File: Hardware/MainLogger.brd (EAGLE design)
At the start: 98.9 x 72.1 mm, 258 parts, among them J3 GEMS_POWER_PLUGINPUT_RT, J4 U.FL, J5 SIM_CDNANO_SF72, P1:C1 0.1uF, P1:C2 2.2uF, P1:C3 1uF, P1:C4 100uF, P1:C5 0.1uF, P1:J1 CONN_TALON_LOGGER, P1:R2 1k, P1:R3 1k, P1:U1 SN74AUP1G08DCK, P1:U2 FXMAR2102UMLP, P1:U3 FSA2258, P1:U4 AP2411, P2:C1 0.1uF, P2:C2 2.2uF, P2:C3 1uF, P2:C4 100uF, P2:C5 0.1uF, P2:J1 CONN_TALON_LOGGER, P2:R2 1k, P2:R3 1k, P2:U1 SN74AUP1G08DCK, P2:U2 FXMAR2102UMLP, P2:U3 FSA2258, P2:U4 AP2411, P3:C1 0.1uF, P3:C2 2.2uF, P3:C3 1uF, P3:C4 100uF, P3:C5 0.1uF, P3:J1 CONN_TALON_LOGGER, P3:R2 1k, P3:R3 1k, P3:U1 SN74AUP1G08DCK, P3:U2 FXMAR2102UMLP, P3:U3 FSA2258, P3:U4 AP2411, P4:C1 0.1uF, P4:C2 2.2uF, P4:C3 1uF, P4:C4 100uF, P4:C5 0.1uF, P4:J1 CONN_TALON_LOGGER, P4:R2 1k, P4:R3 1k, P4:U1 SN74AUP1G08DCK, P4:U2 FXMAR2102UMLP, P4:U3 FSA2258, P4:U4 AP2411, Q1 DMG3404, Q2 MOSFET_PCH-DMP3036SFG, Q3 MOSFET_PCH-DMP3036SFG, Q4 DMG3404, Q5 NX2301P, Q6 NX2301P, U1 FXMAR2102UMLP, U10 SN74AUP3G34DCU, U11 TCK111G, U12 LTC4412S6, U13 TCR2LE31ESV, U14 LP59073.3VYKE, U15 MIC22602, U16 BQ25616, U17 TPS61282D, U18 MCP23018QFN, U19 MCP23018QFN, U2 VEML3328, U20 MAX-M8W, U21 MCP79412SOIC, U22 HALL_EFFECT_SI7201, U23 PCA9634QFN, U24 SN74LVC1G17DCK, U25 TPL5010DDC, U26 TPL5010DDC, U27 MB85RC, U28 FXMAR2102UMLP, U29 SIT1552, U3 MMC5633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

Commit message: v1.5 Update
Updated schematic and layout, boards sent to fab
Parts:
- removed R43: 130k, bschulz_passives:R0402
- removed R44: 30k, bschulz_passives:R0402
- R38: value 150k -> 100k
- R39: value 10k -> 100k
- U18, U19: value MCP23018QFN -> PCAL9535AQFN
- moved R38 16.2 mm to (38.6, 31.4)
- moved C39 3.84 mm to (43.2, 29.1)
- moved R39 1.85 mm to (48.4, 43.6), turned to 0 degrees
- moved C38 1.14 mm to (51.4, 43.6), turned to 0 degrees
- moved U19 0.89 mm to (39.0, 26.7), turned to 0 degrees
- moved U18 0.13 mm to (49.5, 39.5), turned to 0 degrees
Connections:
- removed net N$35: R43.1, R44.2, U19.11
- removed net N$38: R38.1, R39.2, U18.11
- net !CE: now also U18.13; no longer U18.3
- net !RESET: no longer U18.12, U19.12
- net !TALON1_FAULT: now also U19.3; no longer U19.17
- net !TALON2_FAULT: now also U19.7; no longer U19.21
- net !TALON3_FAULT: now also U19.12; no longer U19.2
- net !TALON4_FAULT: now also U19.16; no longer U19.6
- net 3V3_AUX_EN: now also U18.17; no longer U18.7
- net 3V3_AUX_PG: now also U18.1; no longer U18.15
- net 3V3_CORE: now also R39.2, U18.21, U19.18, U19.21; no longer R43.2, U18.8, U19.8
- net 3V3_SD_EN: now also U18.14; no longer U18.4
- net CHG_SOURCE: now also U18.7; no longer U18.21
- net CSA_EN: now also U18.16; no longer U18.6
- net GND: now also U18.18, U18.24, U18.9, U19.24, U19.9; no longer R39.1, R44.1
- net GPS_INT: now also U18.8; no longer U18.22
- net I2C_EXT_EN: now also U18.12; no longer U18.2
- net LED_EN: now also U18.15; no longer U18.5
- net N$6: now also U18.5; no longer U18.19
- net N$8: now also U18.6; no longer U18.20
- net N$9: now also U18.4; no longer U18.18
- net OB_INT: now also R39.1, U18.22; no longer U18.14
- net SCL_OB: now also U18.19, U19.19; no longer U18.9, U19.9
- net SDA_OB: now also U18.20, U19.20; no longer U18.10, U19.10
- net SD_CD: now also U18.10; no longer U18.24
- net SENSOR_INT: now also U18.3; no longer U18.17
- net SIM_CD: now also U18.11; no longer U18.1
- net TALON1_EN: now also U19.4; no longer U19.18
- net TALON1_I2C_EN: now also U19.2; no longer U19.16
- net TALON1_SEL: now also U19.1; no longer U19.15
- net TALON2_EN: now also U19.8; no longer U19.22
- net TALON2_I2C_EN: now also U19.6; no longer U19.20
- net TALON2_SEL: now also U19.5; no longer U19.19
- net TALON3_EN: now also U19.13; no longer U19.3
- net TALON3_I2C_EN: now also U19.11; no longer U19.1
- net TALON3_SEL: now also U19.10; no longer U19.24
- net TALON4_EN: now also U19.17; no longer U19.7
- net TALON4_I2C_EN: now also U19.15; no longer U19.5
- net TALON4_SEL: now also U19.14; no longer U19.4
- net TALON_INT: now also R38.1, U19.22; no longer U19.14
- net VBULK_PG: now also U18.2; no longer U18.16
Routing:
- net !RESET: track 118.6 -> 72.3 mm, vias 5 -> 2
- net GND: track 944.7 -> 940.3 mm
- net N$38: track 4.19 -> 0.00 mm
- net N$35: track 4.01 -> 0.00 mm
- net OB_INT: track 36.5 -> 33.6 mm
- net TALON_INT: track 71.6 -> 69.2 mm
- net SD_CD: track 68.3 -> 66.0 mm
- net SCL_OB: track 172.5 -> 170.3 mm
- net TALON2_SEL: track 21.0 -> 23.2 mm
- net TALON4_EN: track 43.1 -> 41.0 mm
- net SDA_OB: track 173.0 -> 170.9 mm
- net CSA_EN: track 90.6 -> 92.7 mm
- net 3V3_AUX_EN: track 72.0 -> 73.8 mm
- net SIM_CD: track 29.6 -> 31.1 mm
- net TALON3_I2C_EN: track 27.2 -> 28.6 mm
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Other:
- board text added: "Project Kestrel v1.5 Bobby Schulz"
- board text removed: "Project Kestrel v1.4 Bobby Schulz"

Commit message: v1.6 Update
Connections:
- net BAT_CHG: no longer C49.1, D4.2, R54.1, R55.1, U24.5, U25.1
- net SYSCORE: now also C49.1, D4.2, R54.1, R55.1, U24.5, U25.1
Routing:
- net BAT_CHG: track 120.6 -> 23.3 mm, vias 7 -> 2
- net SYSCORE: track 55.9 -> 123.4 mm, vias 2 -> 6
- net 3V3_CORE: track 343.6 -> 343.0 mm
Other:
- board text added: "Project Kestrel v1.6 Bobby Schulz"
- board text removed: "Project Kestrel v1.5 Bobby Schulz"

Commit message: Added fix for WDT
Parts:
- TP1, TP2, TP5, TP6, TP7, TP8, TP9: value TESTPOINTRCU -> TESTPOINT_DNP_RCU
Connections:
- net GND: now also U26.4
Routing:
- net GND: track 940.3 -> 941.7 mm
- net N$12: track 14.0 -> 13.4 mm
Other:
- board text added: "H5"
- board text added: "Project Kestrel v1.7 Bobby Schulz"
- board text removed: "Project Kestrel v1.6 Bobby Schulz"

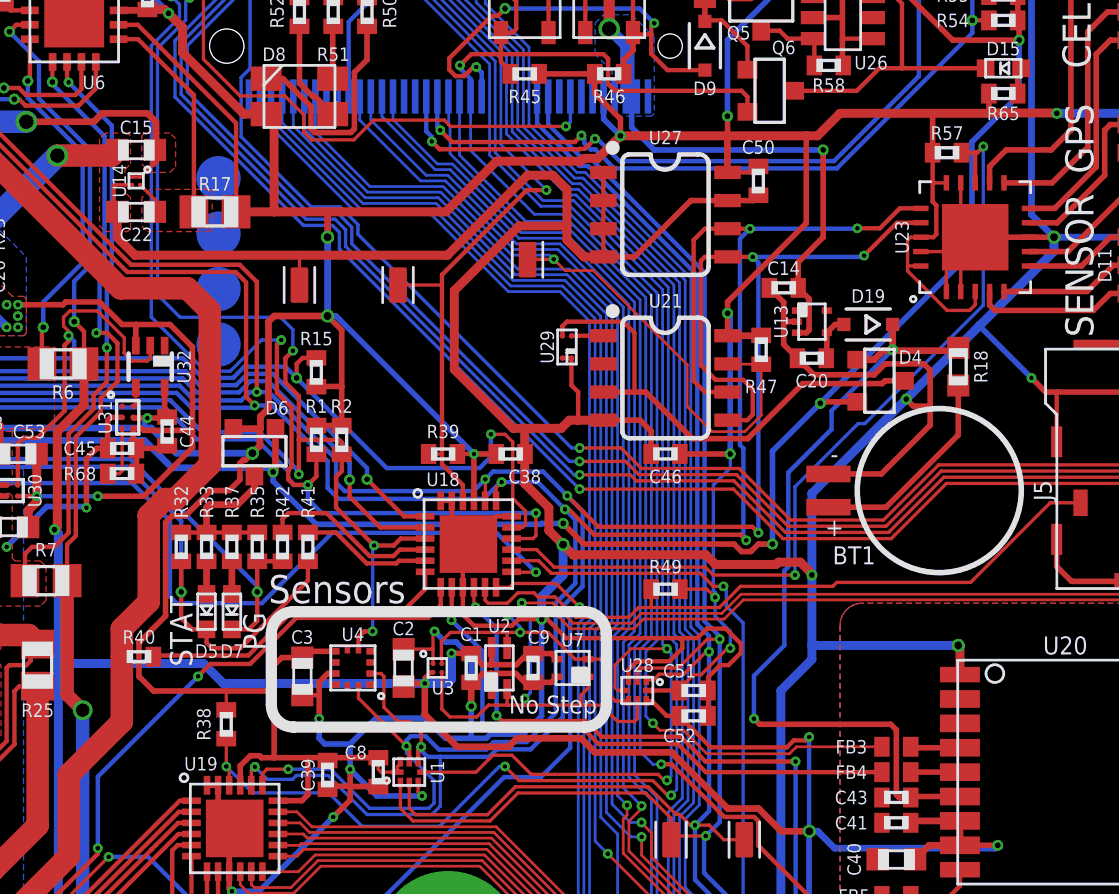
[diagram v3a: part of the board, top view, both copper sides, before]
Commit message: v1.8 Updates
- Changed accel (#1)
- Fixed backup regulator issue (#16)
- Fixed TCXO overvoltage issue (#19)
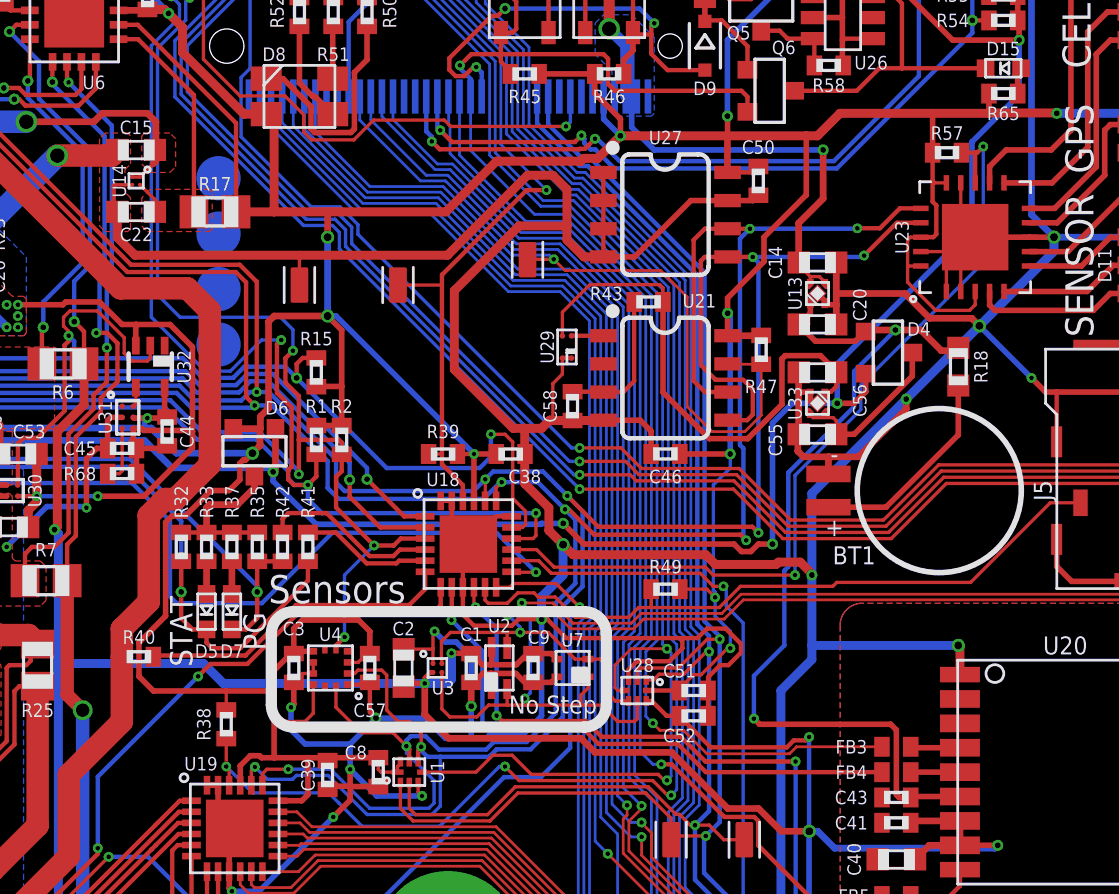
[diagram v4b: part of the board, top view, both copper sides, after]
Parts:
- removed D19: (no value), bschulz:SOD323-R
- added C55, C56: 1uF, bschulz_passives:C0603
- added C57: 0.1uF, bschulz_passives:C0402
- added C58: 100pF, bschulz_passives:C0402
- added R43: 1k, bschulz_passives:R0402
- added U33: TPS7A0218PDQ, bschulz:X2SON
- C14, C20: value 0.1uF -> 1uF; device bschulz_passives:C0402 -> bschulz_passives:C0603
- C3: value 2.2uF -> 0.1uF; device bschulz_passives:C0603 -> bschulz_passives:C0402
- D11, D14, D17, D7: value LEDAMBER0603 -> LEDYELLOW0603
- U13: value TCR2LE31ESV -> TPS7A0331PDQ; device bschulz:SOT-553 -> bschulz:X2SON
- U4: value MXC6655 -> BMA456
- moved C14 1.91 mm to (65.3, 52.2), turned to 0 degrees
- moved C20 1.55 mm to (65.3, 49.4), turned to 0 degrees
- moved D4 1.33 mm to (68.5, 48.1)
- moved U13 1.30 mm to (65.3, 50.8), turned to 90 degrees
- moved U4 1.02 mm to (43.3, 33.9)
- moved C3 0.54 mm to (41.7, 33.9)
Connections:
- net N$4 renamed CLK_OSC
- removed net N$3: C20.1, D19.A, U13.4
- new net BCKP_PRIME: C55.1, D4.3, U33.3, U33.4
- new net VDD_CLK: C56.1, R43.1, U29.3, U33.1
- net 3V3_CORE: now also C57.1, U4.10, U4.3
- net BCKP_GPS: now also C20.1, U13.1; no longer D19.C
- net BCKP_RTC: now also C58.1, R43.2; no longer D4.3, U29.3
- net GND: now also C55.2, C56.2, C57.2, C58.2, U13.EP, U33.2, U33.EP, U4.1, U4.8
- net VBULK: now also U13.4; no longer U13.1
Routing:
- net VDD_CLK: track 0.00 -> 23.9 mm
- net BCKP_RTC: track 22.2 -> 6.56 mm
- net 3V3_CORE: track 343.0 -> 352.7 mm
- net BCKP_PRIME: track 0.00 -> 7.63 mm
- net GND: track 941.7 -> 948.5 mm, vias 59 -> 61
- net BCKP_GPS: track 37.7 -> 42.0 mm
- net VBULK: track 148.0 -> 145.4 mm
- net N$3: track 2.08 -> 0.00 mm
- net SYSCORE: track 123.4 -> 125.2 mm
- net RTC_INT: track 33.7 -> 35.5 mm
- net SCL_OB: track 170.3 -> 171.6 mm
- net SDA_OB: track 170.9 -> 172.2 mm
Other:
- board text added: "Project Kestrel v1.8 Bobby Schulz"
- board text added: "SYS"
- board text removed: "Project Kestrel v1.7 Bobby Schulz"

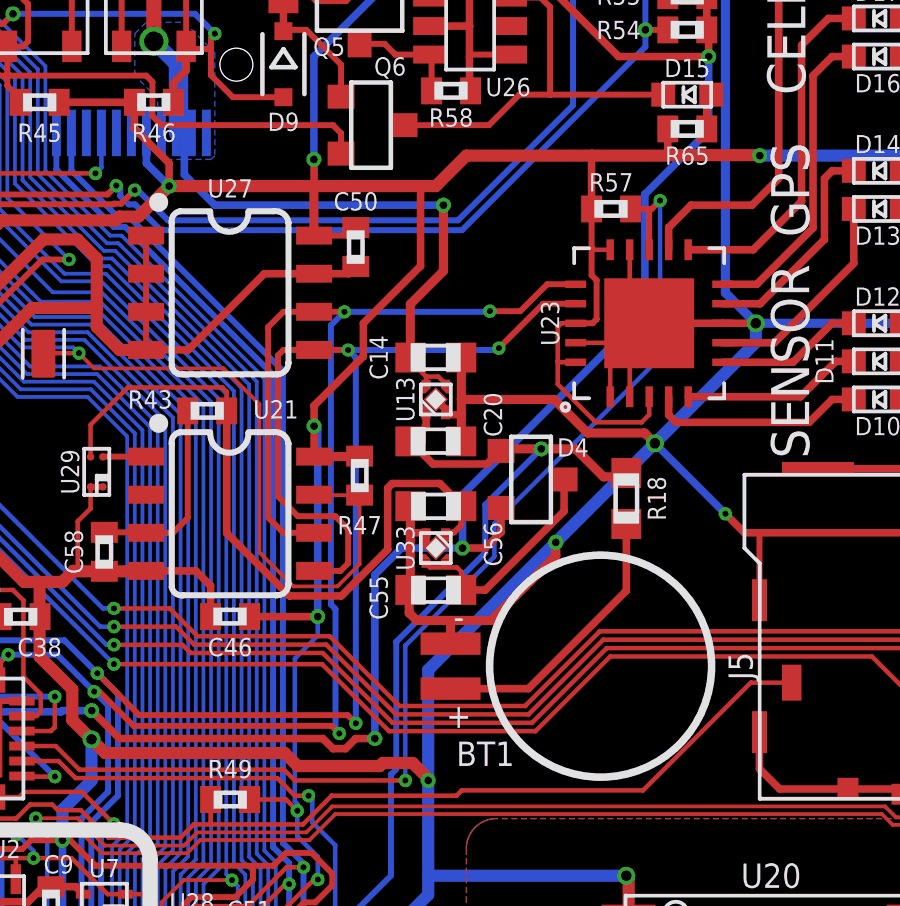
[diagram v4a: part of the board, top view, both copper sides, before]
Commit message: v1.9 updates
Added series diode in gps/rtc bat charger to prevent reverse current
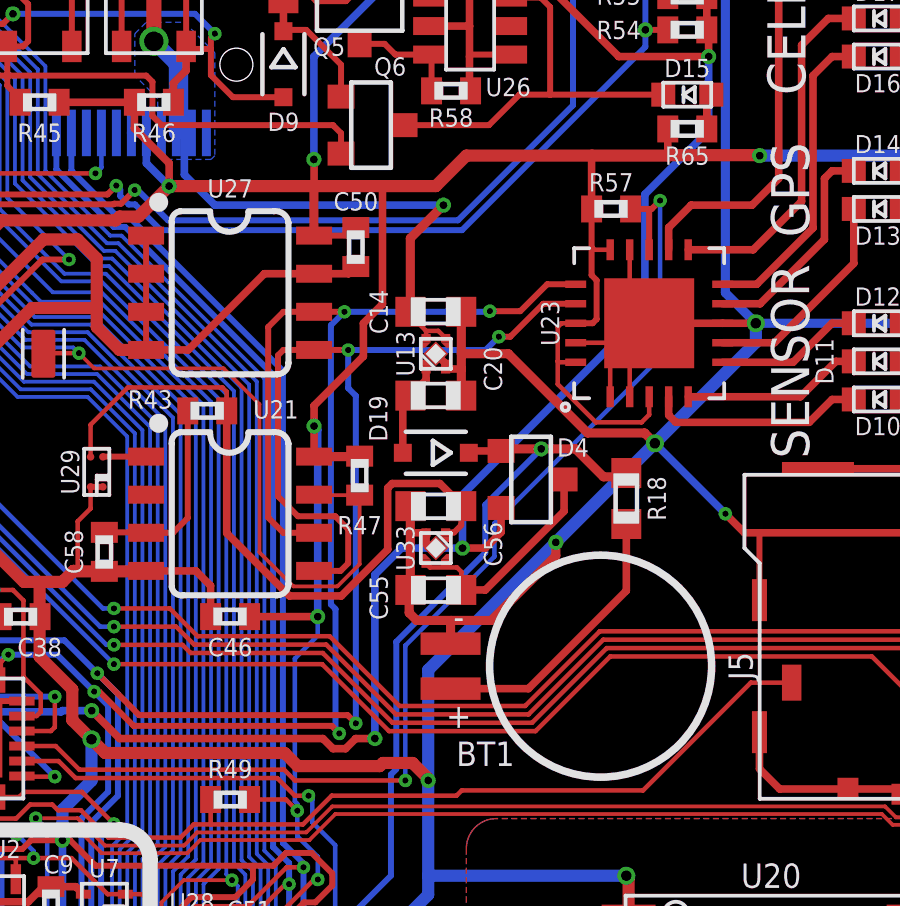
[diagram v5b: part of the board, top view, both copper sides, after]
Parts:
- added D19: BAT54WS, bschulz:SOD323-R
- moved C20 1.52 mm to (65.3, 50.9)
- moved U13 1.52 mm to (65.3, 52.3)
- moved C14 1.52 mm to (65.3, 53.7)
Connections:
- new net BCKP_GPS_REG: C20.1, D19.A, U13.1
- net BCKP_GPS: now also D19.C; no longer C20.1, U13.1
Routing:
- net BCKP_GPS: track 42.0 -> 38.8 mm
- net BCKP_GPS_REG: track 0.00 -> 3.10 mm
- net VBULK: track 145.4 -> 143.9 mm
- net GND: track 948.5 -> 949.2 mm
- net 3V3_CORE: track 352.7 -> 352.1 mm
